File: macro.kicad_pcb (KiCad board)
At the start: 2 copper layers, 77 x 38.1 mm, 27 parts, among them J1 USB_C_Receptacle_USB2.0, SW1 SW_Push, U1 ATmega32U4-A, Y1 16MHz

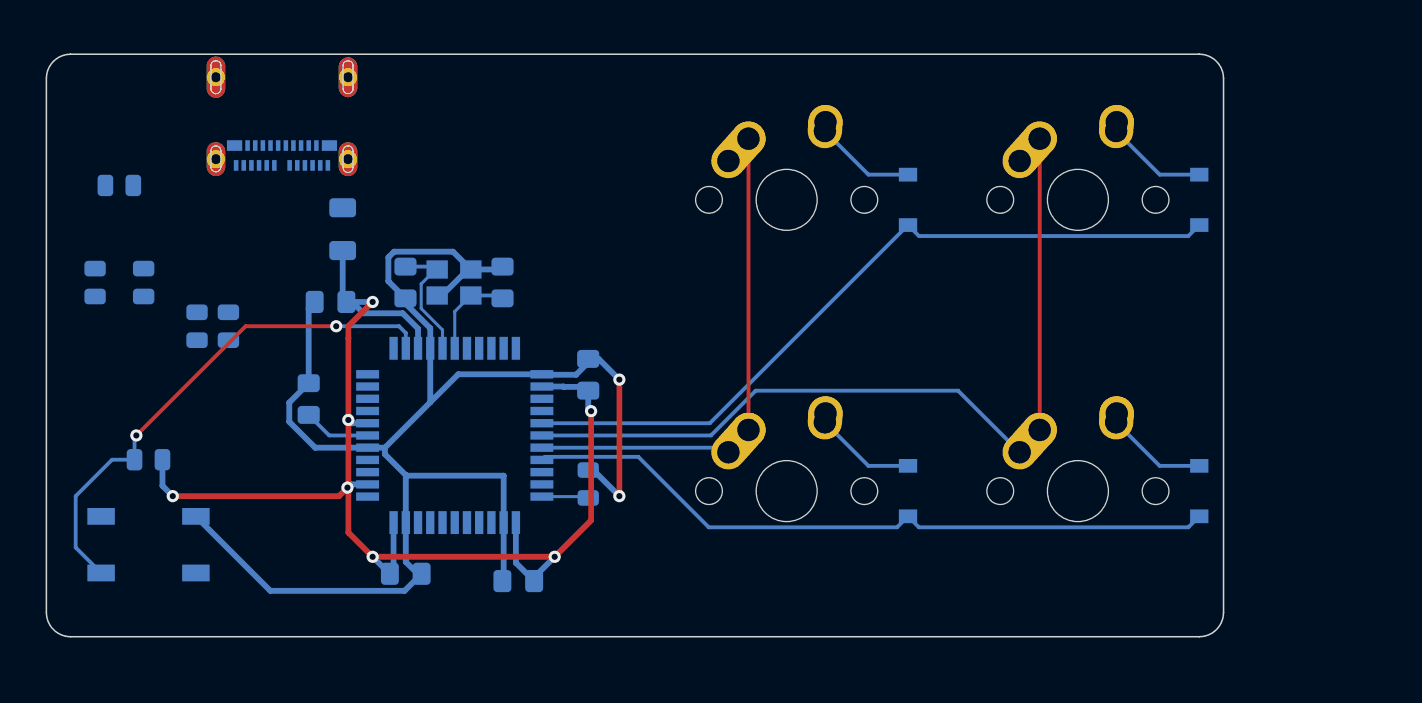
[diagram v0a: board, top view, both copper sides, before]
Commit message: Add ws2812
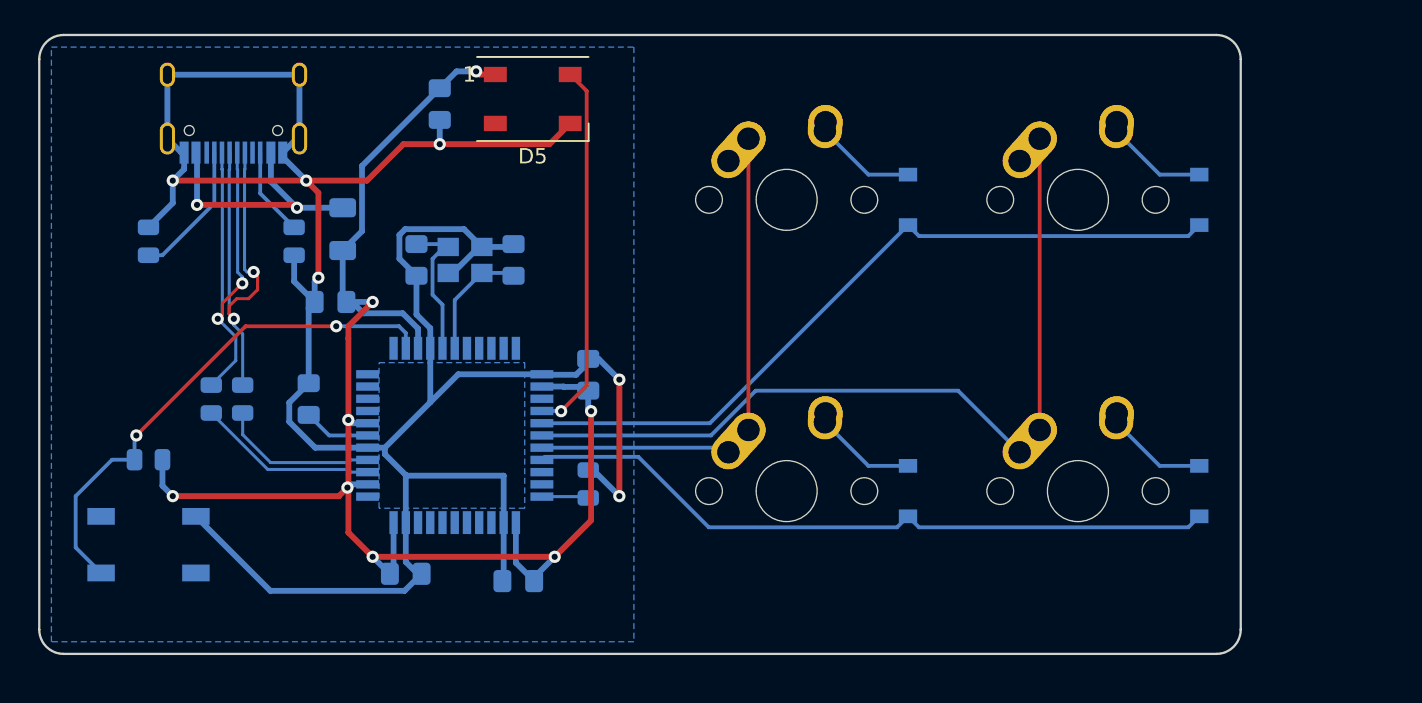
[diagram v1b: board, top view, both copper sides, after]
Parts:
- removed J1: USB_C_Receptacle_USB2.0, 105450-0101:MOLEX_105450-0101
- removed R7: 1M, Resistor_SMD:R_0805_2012Metric
- added C8: 0.1uF, Capacitor_SMD:C_0805_2012Metric_Pad1.18x1.45mm_HandSolder, B.Cu at (131.8, 82.3)
- added D5: WS2812B, LED_SMD:LED_WS2812B_PLCC4_5.0x5.0mm_P3.2mm, F.Cu at (137.8, 82.0)
- added USB1: TYPE-C-31-M-12, Type-C:HRO-TYPE-C-31-M-12-Assembly, B.Cu at (118.3, 77.8)
- moved R6 10.2 mm to (122.2, 91.3)
- moved R1 4.85 mm to (118.9, 101.6)
- moved R2 4.85 mm to (116.8, 101.6)
- moved R5 4.41 mm to (112.7, 91.3), turned to 90 degrees
- moved C3 1.64 mm to (136.6, 92.5)
- moved Y1 1.64 mm to (133.4, 92.5)
- moved C2 1.64 mm to (130.2, 92.5)
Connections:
- F1 pad 1: VCC -> VBUS
- R1 pad 2: Net-(R1-Pad2) -> D+
- R2 pad 2: Net-(R2-Pad2) -> D-
- U1 pad 26: unconnected-(U1-Pad26) -> LED_DIN
- U1 pad 3: Net-(R2-Pad2) -> D-
- U1 pad 4: Net-(R1-Pad2) -> D+
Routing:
- net GND: track 106.7 -> 177.3 mm, vias 2 -> 6
- net D-: track 0.00 -> 40.0 mm, vias 0 -> 2
- net D+: track 0.00 -> 38.8 mm, vias 0 -> 2
- net LED_DIN: track 0.00 -> 24.4 mm, vias 0 -> 1
- net +5V: track 85.8 -> 103.2 mm, vias 7 -> 8
- net VBUS: track 0.00 -> 17.4 mm, vias 0 -> 2
- net Net-(R5-Pad1): track 0.00 -> 9.03 mm
- net Net-(R6-Pad1): track 0.00 -> 5.81 mm
- net Net-(C3-Pad2): track 6.04 -> 7.82 mm
- net Net-(C2-Pad2): track 8.38 -> 9.62 mm
- added copper zone on B.Cu, net GND
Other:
- board size 77 x 38.1 mm -> 78.6 x 40.5 mm
- board text added: "Macroboard v0.1 Designed and built by Nick Yu"

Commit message: New design
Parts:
- added C9: 0.1uF, Capacitor_SMD:C_0805_2012Metric_Pad1.18x1.45mm_HandSolder, B.Cu at (124.6, 101.6)
- added H1: MountingHole, MountingHole:MountingHole_2.2mm_M2, F.Cu at (185.7, 115.1)
- added H2: MountingHole, MountingHole:MountingHole_2.2mm_M2, F.Cu at (108.7, 115.1)
- added H3: MountingHole, MountingHole:MountingHole_2.2mm_M2, F.Cu at (185.7, 81.0)
- added H4: MountingHole, MountingHole:MountingHole_2.2mm_M2, F.Cu at (108.7, 81.0)
- moved R2 7.40 mm to (116.7, 94.2)
- moved R1 7.40 mm to (118.8, 94.2)
- moved R3 5.02 mm to (111.1, 110.3)
- moved SW1 5.00 mm to (111.2, 106.4)
- moved R4 4.80 mm to (142.1, 111.9), turned to -90 degrees
- moved C7 3.20 mm to (123.6, 98.4), turned to 0 degrees
- moved R5 2.25 mm to (114.3, 89.7)
- moved C5 1.63 mm to (136.5, 111.9)
- moved C1 1.28 mm to (130.2, 111.9)
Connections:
- USB1 pad 13: GND -> unconnected-(USB1-Pad13)
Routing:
- net GND: track 177.3 -> 146.9 mm
- net VBUS: track 17.4 -> 34.0 mm
- net D-: track 40.0 -> 28.7 mm, vias 2 -> 0
- net D+: track 38.8 -> 28.2 mm, vias 2 -> 0
- net Net-(C7-Pad1): track 4.41 -> 9.00 mm
- net Net-(R3-Pad2): track 34.0 -> 38.1 mm
- net Net-(R5-Pad1): track 9.03 -> 6.78 mm
- net +5V: track 103.2 -> 101.1 mm, vias 8 -> 7
- net Net-(R4-Pad1): track 3.07 -> 4.89 mm
- net LED_DIN: track 24.4 -> 25.1 mm
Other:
- board size 78.6 x 40.5 mm -> 83 x 40.5 mm

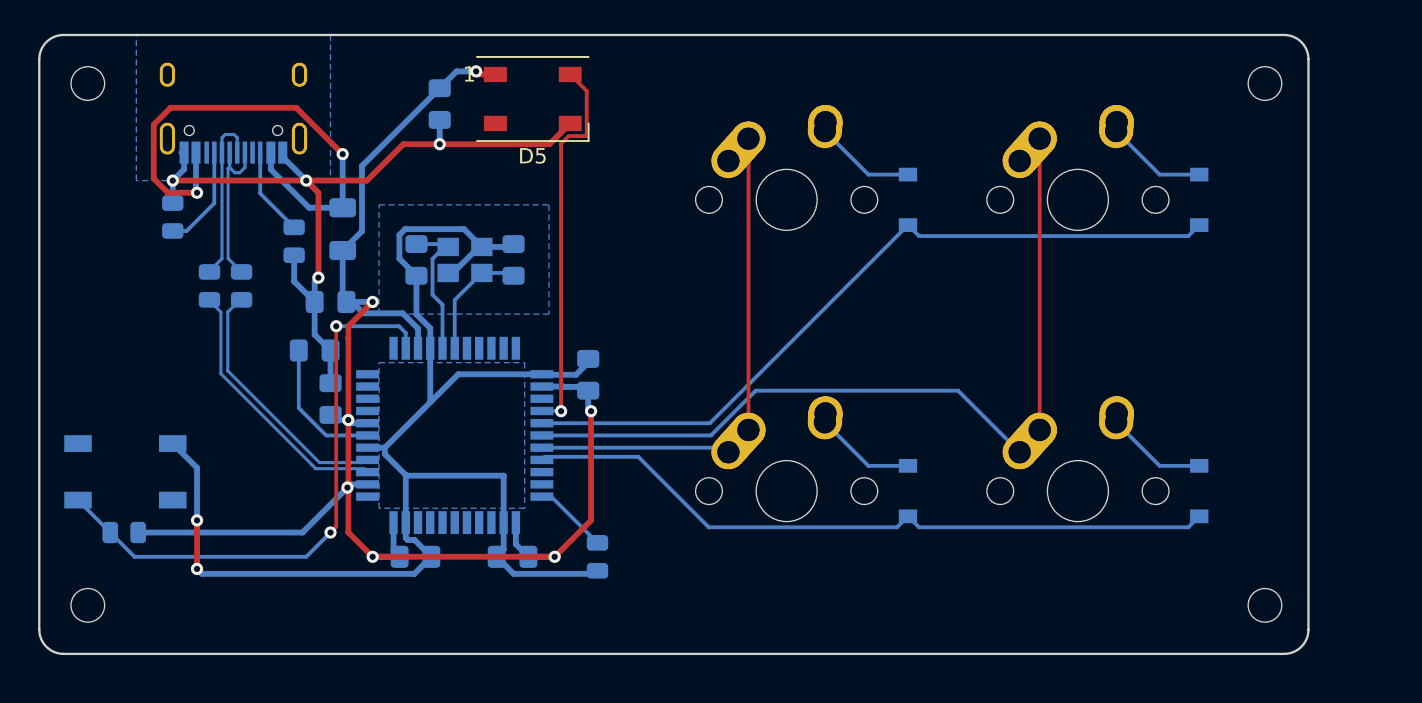
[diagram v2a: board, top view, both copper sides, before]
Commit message: Rough placement
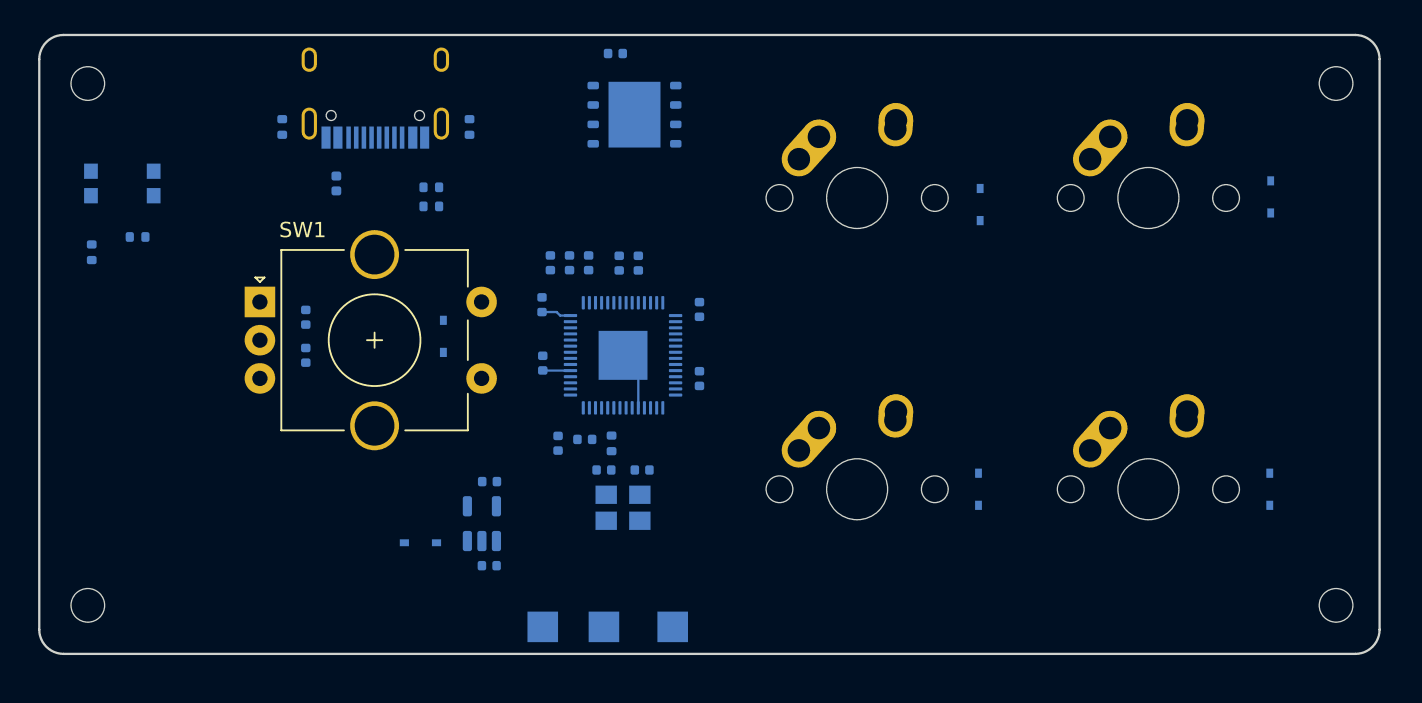
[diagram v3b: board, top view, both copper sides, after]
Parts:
- removed the D5 at (137.8, 82.0)
- added C10: 100nF, Capacitor_SMD:C_0402_1005Metric, B.Cu at (148.8, 95.7)
- added C11: 100nF, Capacitor_SMD:C_0402_1005Metric, B.Cu at (138.5, 99.2)
- added C12: 100nF, Capacitor_SMD:C_0402_1005Metric, B.Cu at (141.2, 104.2)
- added C13: 100nF, Capacitor_SMD:C_0402_1005Metric, B.Cu at (140.2, 92.7)
- added C14: 100nF, Capacitor_SMD:C_0402_1005Metric, B.Cu at (148.8, 100.3)
- added C15: 1uF, Capacitor_SMD:C_0402_1005Metric, B.Cu at (139.0, 92.7)
- added C16: 1uF, Capacitor_SMD:C_0402_1005Metric, B.Cu at (141.5, 92.7)
- added C17: 100nF, Capacitor_SMD:C_0402_1005Metric, B.Cu at (139.5, 104.5)
- added C18: 100nF, Capacitor_SMD:C_0402_1005Metric, B.Cu at (144.8, 92.7)
- added D3: D_Small, Diode_SMD:D_SOD-323, B.Cu at (186.1, 88.4)
- added D6: D_Small, Diode_SMD:D_SOD-323, B.Cu at (132.0, 97.5)
- added J1: Conn_01x01_Male, TestPoint:TestPoint_Pad_2.0x2.0mm, B.Cu at (147.0, 116.5)
- added J2: Conn_01x01_Male, TestPoint:TestPoint_Pad_2.0x2.0mm, B.Cu at (138.5, 116.5)
- added J3: Conn_01x01_Male, TestPoint:TestPoint_Pad_2.0x2.0mm, B.Cu at (142.5, 116.5)
- added R7: 1K, Resistor_SMD:R_0402_1005Metric, B.Cu at (143.0, 104.5)
- added SW2: SW_Push, Button_Switch_SMD:SW_Push_1P1T_NO_CK_KMR2, B.Cu at (111.0, 87.5)
- added U2: W25Q128JVPIQ, Package_SON:WSON-8-1EP_6x5mm_P1.27mm_EP3.4x4.3mm, B.Cu at (144.5, 83.0)
- added U3: RP2040, Package_DFN_QFN:QFN-56-1EP_7x7mm_P0.4mm_EP3.2x3.2mm, B.Cu at (143.8, 98.7)
- C1, C2: value 0.1uF -> 10uF; footprint Capacitor_SMD:C_0805_2012Metric_Pad1.18x1.45mm_HandSolder -> Capacitor_SMD:C_0402_1005Metric
- C3, C8, C9: value 0.1uF -> 100nF; footprint Capacitor_SMD:C_0805_2012Metric_Pad1.18x1.45mm_HandSolder -> Capacitor_SMD:C_0402_1005Metric
- C4, C5: value 0.1uF -> 10nF; footprint Capacitor_SMD:C_0805_2012Metric_Pad1.18x1.45mm_HandSolder -> Capacitor_SMD:C_0402_1005Metric
- C6: value 10uF -> 30pF; footprint Capacitor_SMD:C_0805_2012Metric_Pad1.18x1.45mm_HandSolder -> Capacitor_SMD:C_0402_1005Metric
- C7: value 1uF -> 30pF; footprint Capacitor_SMD:C_0805_2012Metric_Pad1.18x1.45mm_HandSolder -> Capacitor_SMD:C_0402_1005Metric
- D1: value D_Small -> D_Schottky_Small; footprint Diode_SMD:D_SOD-123 -> Diode_SMD:D_SOD-323
- D2: footprint Diode_SMD:D_SOD-123 -> Diode_SMD:D_SOD-323
- D4: renamed from D3; footprint Diode_SMD:D_SOD-123 -> Diode_SMD:D_SOD-323
- D5: renamed from D4; footprint Diode_SMD:D_SOD-123 -> Diode_SMD:D_SOD-323
- F1: footprint Fuse:Fuse_1206_3216Metric -> Fuse:Fuse_0402_1005Metric
- R1, R2: value 22 -> 5.1k; footprint Resistor_SMD:R_0805_2012Metric -> Resistor_SMD:R_0402_1005Metric
- R3: footprint Resistor_SMD:R_0805_2012Metric -> Resistor_SMD:R_0402_1005Metric
- R4: value 10k -> 1K; footprint Resistor_SMD:R_0805_2012Metric -> Resistor_SMD:R_0402_1005Metric
- R5, R6: value 5.1k -> 27.4; footprint Resistor_SMD:R_0805_2012Metric -> Resistor_SMD:R_0402_1005Metric
- SW1: value SW_Push -> RotaryEncoder_Switch; footprint random-keyboard-parts:SKQG-1155865 -> Rotary_Encoder:RotaryEncoder_Alps_EC11E-Switch_Vertical_H20mm_CircularMountingHoles; moved to F.Cu
- U1: value ATmega32U4-A -> AP2112K-3.3; footprint Package_QFP:TQFP-44_10x10mm_P0.8mm -> Package_TO_SOT_SMD:SOT-23-5
- Y1: value 16MHz -> 12MHz
- moved D1 39.0 mm to (130.5, 111.0), turned to 180 degrees
- moved R4 38.6 mm to (109.0, 92.0)
- moved C6 23.2 mm to (145.0, 106.2)
- moved C7 20.5 mm to (142.5, 106.2)
- moved R2 19.9 mm to (133.7, 83.8)
- moved R3 19.4 mm to (112.0, 91.0), turned to 0 degrees
- moved Y1 19.2 mm to (143.8, 108.7)
- moved C5 18.9 mm to (123.0, 98.7), turned to -90 degrees
- moved C4 18.9 mm to (123.0, 96.2), turned to -90 degrees
- moved R5 17.0 mm to (131.2, 87.8), turned to 0 degrees
- moved C8 15.7 mm to (143.5, 92.7), turned to 90 degrees
- moved C2 15.3 mm to (135.0, 107.0), turned to 180 degrees
- moved C9 15.1 mm to (138.4, 95.4)
- moved C3 15.1 mm to (143.2, 79.0), turned to 0 degrees
- moved D2 14.3 mm to (167.1, 88.9)
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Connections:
- C1 pad 1: +5V -> Net-(C1-Pad1)
- C2 pad 1: GND -> +3.3V
- C2 pad 2: Net-(C2-Pad2) -> GND
- C3 pad 1: GND -> +3.3V
- C3 pad 2: Net-(C3-Pad2) -> GND
- C4 pad 1: +5V -> ROT0
- C5 pad 1: +5V -> GND
- C5 pad 2: GND -> ROT1
- C6 pad 1: +5V -> GND
- C6 pad 2: GND -> XIN
- C7 pad 1: Net-(C7-Pad1) -> GND
- C7 pad 2: GND -> Net-(C7-Pad2)
- C8 pad 1: +5V -> +3.3V
- C9 pad 1: +5V -> +3.3V
- D1 pad 1: ROW0 -> Net-(C1-Pad1)
- F1 pad 2: +5V -> Net-(D1-Pad2)
- MX1 pad 2: Net-(D1-Pad2) -> Net-(D2-Pad2)
- MX2 pad 2: Net-(D2-Pad2) -> Net-(D3-Pad2)
- R1 pad 1: D+ -> Net-(R1-Pad1)
- R1 pad 2: D+ -> GND
- R2 pad 1: D- -> Net-(R2-Pad1)
- R2 pad 2: D- -> GND
- R3 pad 1: +5V -> +3.3V
- R3 pad 2: Net-(R3-Pad2) -> QSPI_SS
- R4 pad 1: Net-(R4-Pad1) -> BOOTSEL
- R4 pad 2: GND -> QSPI_SS
- R5 pad 1: Net-(R5-Pad1) -> D+
- R5 pad 2: GND -> Net-(R5-Pad2)
- R6 pad 1: Net-(R6-Pad1) -> D-
- R6 pad 2: GND -> Net-(R6-Pad2)
- U1 pad 1: unconnected-(U1-Pad1) -> Net-(C1-Pad1)
- U1 pad 2: +5V -> GND
- U1 pad 3: D- -> Net-(C1-Pad1)
- U1 pad 4: D+ -> unconnected-(U1-Pad4)
- U1 pad 5: GND -> +3.3V
- USB1 pad 10: Net-(R6-Pad1) -> Net-(R2-Pad1)
- USB1 pad 4: Net-(R5-Pad1) -> Net-(R1-Pad1)
- Y1 pad 1: Net-(C2-Pad2) -> Net-(C7-Pad2)
- Y1 pad 3: Net-(C3-Pad2) -> XIN
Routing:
- net GND: track 146.9 -> 3.85 mm, vias 6 -> 0
- net +5V: track 101.1 -> 0.00 mm, vias 7 -> 0
- net COL1: track 54.8 -> 1.59 mm
- net ROW0: track 49.0 -> 0.00 mm
- net ROW1: track 45.9 -> 0.00 mm
- net Net-(R3-Pad2): track 38.1 -> 0.00 mm, vias 2 -> 0
- net VBUS: track 34.0 -> 0.00 mm, vias 2 -> 0
- net COL0: track 31.4 -> 0.42 mm
- net D-: track 28.7 -> 0.00 mm
- net D+: track 28.2 -> 0.00 mm
- net LED_DIN: track 25.1 -> 0.00 mm, vias 1 -> 0
- net Net-(C2-Pad2): track 9.62 -> 0.00 mm
- net Net-(C7-Pad1): track 9.00 -> 0.00 mm
- net Net-(C3-Pad2): track 7.82 -> 0.00 mm
- net Net-(R5-Pad1): track 6.78 -> 0.00 mm
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- removed copper zone on B.Cu, net GND
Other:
- board size 83 x 40.5 mm -> 87.7 x 40.5 mm

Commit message: v0
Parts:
- moved R3 37.4 mm to (147.8, 79.9), turned to 180 degrees
- moved D1 22.2 mm to (126.1, 89.2)
- moved C1 21.4 mm to (131.2, 91.5), turned to -90 degrees
- moved U1 17.8 mm to (133.9, 92.0), turned to 0 degrees
- moved C2 14.6 mm to (136.7, 92.5), turned to 90 degrees
- moved R4 9.47 mm to (116.0, 85.6), turned to 0 degrees
- moved SW2 7.43 mm to (116.0, 82.0), turned to -90 degrees
- moved J3 1.79 mm to (142.9, 114.8)
- moved J2 1.77 mm to (138.8, 114.8)
- moved J1 1.75 mm to (147.0, 114.8)
- moved C17 1.39 mm to (140.8, 104.0), turned to 180 degrees
- moved C3 1.35 mm to (142.3, 80.0)
- moved C12 1.12 mm to (140.8, 105.3), turned to 180 degrees
- moved F1 0.99 mm to (125.1, 86.5)
- moved R5 0.75 mm to (130.7, 87.2)
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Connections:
- R5 pad 2: Net-(R5-Pad2) -> D+
- R6 pad 2: Net-(R6-Pad2) -> D-
- U3 pad 4: ROW1 -> COL1
- U3 pad 46: Net-(R6-Pad2) -> D-
- U3 pad 47: Net-(R5-Pad2) -> D+
- U3 pad 5: COL0 -> ROW1
- U3 pad 6: COL1 -> COL0
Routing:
- net GND: track 3.85 -> 116.4 mm, vias 0 -> 17
- net +3.3V: track 3.77 -> 107.5 mm, vias 0 -> 12
- net COL0: track 0.42 -> 65.1 mm, vias 0 -> 2
- net QSPI_SS: track 0.00 -> 51.7 mm
- net COL1: track 1.59 -> 50.9 mm
- net ROW1: track 0.00 -> 46.7 mm
- net ROW0: track 0.00 -> 42.9 mm
- net D-: track 0.00 -> 28.0 mm
- net D+: track 0.00 -> 27.1 mm
- net ROT0: track 0.00 -> 23.7 mm
- net ROT1: track 0.00 -> 22.6 mm
- net +1V1: track 0.00 -> 21.2 mm
- net SWCLK: track 0.00 -> 17.5 mm, vias 0 -> 2
- net QSPI_SD3: track 0.00 -> 16.0 mm
- net SWD: track 0.00 -> 15.5 mm, vias 0 -> 2
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- added copper zone on B.Cu, net GND
- added copper zone on F.Cu, net GND
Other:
- board text added: "BOOTSEL"
- board text added: "GND"
- board text added: "SWCLK"
- board text added: "SWD"

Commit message: LEDs
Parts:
- added D10: WS2812B, LED_SMD:LED_WS2812B-2020_PLCC4_2.0x2.0mm, B.Cu at (189.0, 89.5)
- added D11: WS2812B, LED_SMD:LED_WS2812B-2020_PLCC4_2.0x2.0mm, B.Cu at (189.0, 98.0)
- added D12: WS2812B, LED_SMD:LED_WS2812B-2020_PLCC4_2.0x2.0mm, B.Cu at (189.0, 107.0)
- added D7: WS2812B, LED_SMD:LED_WS2812B-2020_PLCC4_2.0x2.0mm, B.Cu at (110.0, 89.0)
- added D8: WS2812B, LED_SMD:LED_WS2812B-2020_PLCC4_2.0x2.0mm, B.Cu at (110.0, 97.5)
- added D9: WS2812B, LED_SMD:LED_WS2812B-2020_PLCC4_2.0x2.0mm, B.Cu at (110.0, 106.5)
- added Q1: BSS138, Package_TO_SOT_SMD:SOT-23, B.Cu at (114.5, 91.0)
- added R10: 10k, Resistor_SMD:R_0402_1005Metric, B.Cu at (130.6, 90.8)
- added R8: 10k, Resistor_SMD:R_0402_1005Metric, B.Cu at (117.5, 90.5)
- added R9: 10k, Resistor_SMD:R_0402_1005Metric, B.Cu at (113.5, 88.4)
- added TP1: TestPoint, TestPoint:TestPoint_Pad_D1.0mm, B.Cu at (121.7, 88.3)
- added TP2: TestPoint, TestPoint:TestPoint_Pad_D1.0mm, B.Cu at (129.1, 94.9)
- moved C1 0.96 mm to (131.1, 92.4), turned to 90 degrees
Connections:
- C1 pad 1: Net-(C1-Pad1) -> +5V
- D1 pad 1: Net-(C1-Pad1) -> +5V
- U1 pad 1: Net-(C1-Pad1) -> +5V
- U1 pad 3: Net-(C1-Pad1) -> Net-(R10-Pad2)
- U3 pad 32: unconnected-(U3-Pad32) -> LED_DIN
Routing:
- net +5V: track 0.00 -> 166.1 mm
- net Net-(D12-Pad4): track 0.00 -> 88.9 mm
- net LED_DIN: track 0.00 -> 30.2 mm
- net +3.3V: track 107.5 -> 129.8 mm
- net Net-(C1-Pad1): track 10.7 -> 0.00 mm
- net Net-(D8-Pad2): track 0.00 -> 8.66 mm
- net Net-(D11-Pad4): track 0.00 -> 8.66 mm
- net Net-(D7-Pad4): track 0.00 -> 8.24 mm
- net Net-(D7-Pad2): track 0.00 -> 8.16 mm
- net Net-(D10-Pad4): track 0.00 -> 8.16 mm
- net Net-(R10-Pad2): track 0.00 -> 1.75 mm
- net ROT0: track 23.7 -> 24.9 mm
- net ROW2: track 9.52 -> 10.4 mm
- net GND: track 116.4 -> 116.2 mm, vias 17 -> 22
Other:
- board text added: "+3V"
- board text added: "+5V"

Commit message: Cleanup schematic
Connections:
- net LED_DIN renamed LED_DIN_3V3
- net Net-(D7-Pad4) renamed LED_DIN_5V
- net XIN renamed Net-(C6-Pad2)
- net XOUT renamed Net-(R7-Pad2)
- D10 pad 1: GND -> +5V
- D10 pad 3: +5V -> GND
- D11 pad 1: GND -> +5V
- D11 pad 3: +5V -> GND
- D12 pad 1: GND -> +5V
- D12 pad 3: +5V -> GND
- D7 pad 1: GND -> +5V
- D7 pad 3: +5V -> GND
- D8 pad 1: GND -> +5V
- D8 pad 3: +5V -> GND
- D9 pad 1: GND -> +5V
- D9 pad 3: +5V -> GND
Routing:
- net +5V: track 166.1 -> 156.1 mm, vias 0 -> 2
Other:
- board text added: "Macroboard v0.1"
- board text removed: "Macroboard v0.1 Designed and built by Nick Yu"

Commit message: Add LED decoupling caps
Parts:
- added C19: 100nF, Capacitor_SMD:C_0402_1005Metric, B.Cu at (112.3, 93.7)
- added C20: 100nF, Capacitor_SMD:C_0402_1005Metric, B.Cu at (186.8, 91.3)
- added C21: 100nF, Capacitor_SMD:C_0402_1005Metric, B.Cu at (186.7, 99.9)
- added C22: 100nF, Capacitor_SMD:C_0402_1005Metric, B.Cu at (112.6, 97.6)
- added C23: 100nF, Capacitor_SMD:C_0402_1005Metric, B.Cu at (112.5, 106.6)
- added C24: 100nF, Capacitor_SMD:C_0402_1005Metric, B.Cu at (186.5, 109.9)
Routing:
- net GND: track 116.4 -> 143.3 mm, vias 22 -> 23

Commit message: Update
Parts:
- removed C19, C20, C21, C22, C23, C24: 100nF, Capacitor_SMD:C_0402_1005Metric
